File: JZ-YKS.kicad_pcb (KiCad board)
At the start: 2 copper layers, 50 x 50 mm, 37 parts, among them IC1 JZ4725, U1 PINHEAD30, U2 PINHEAD6, U3 PINHEAD8, X1 CRYSTAL, X2 CRYSTAL

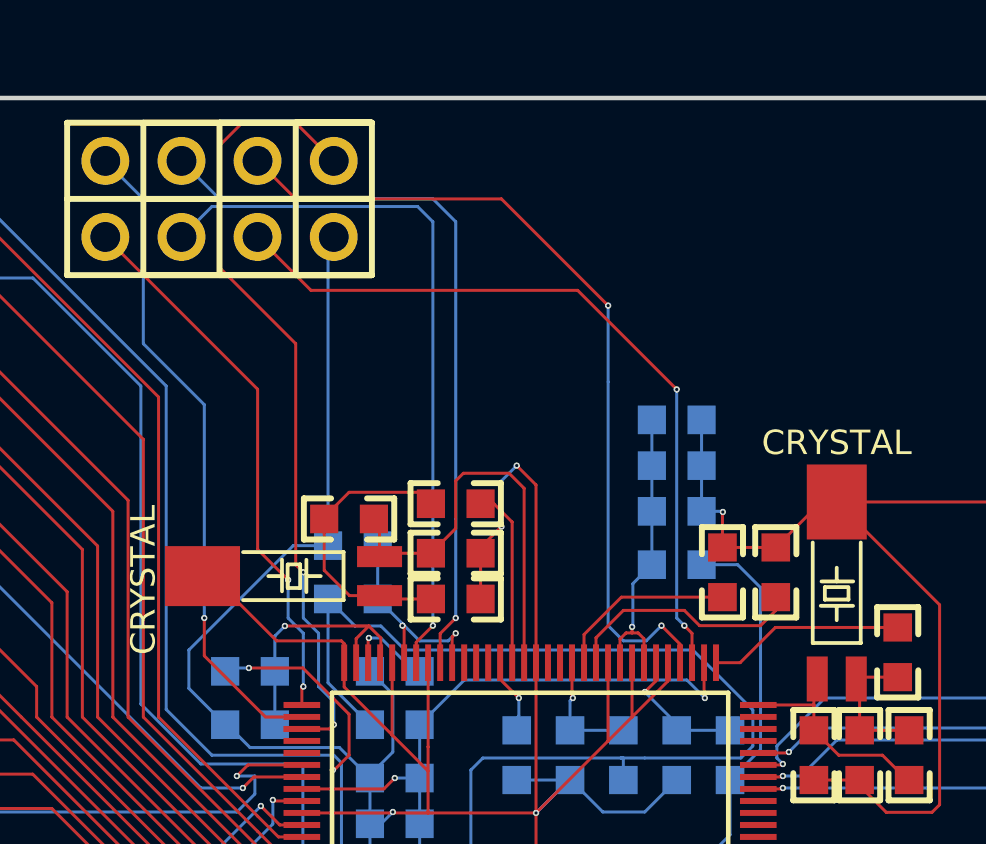
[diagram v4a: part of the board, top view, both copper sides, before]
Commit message: usb added
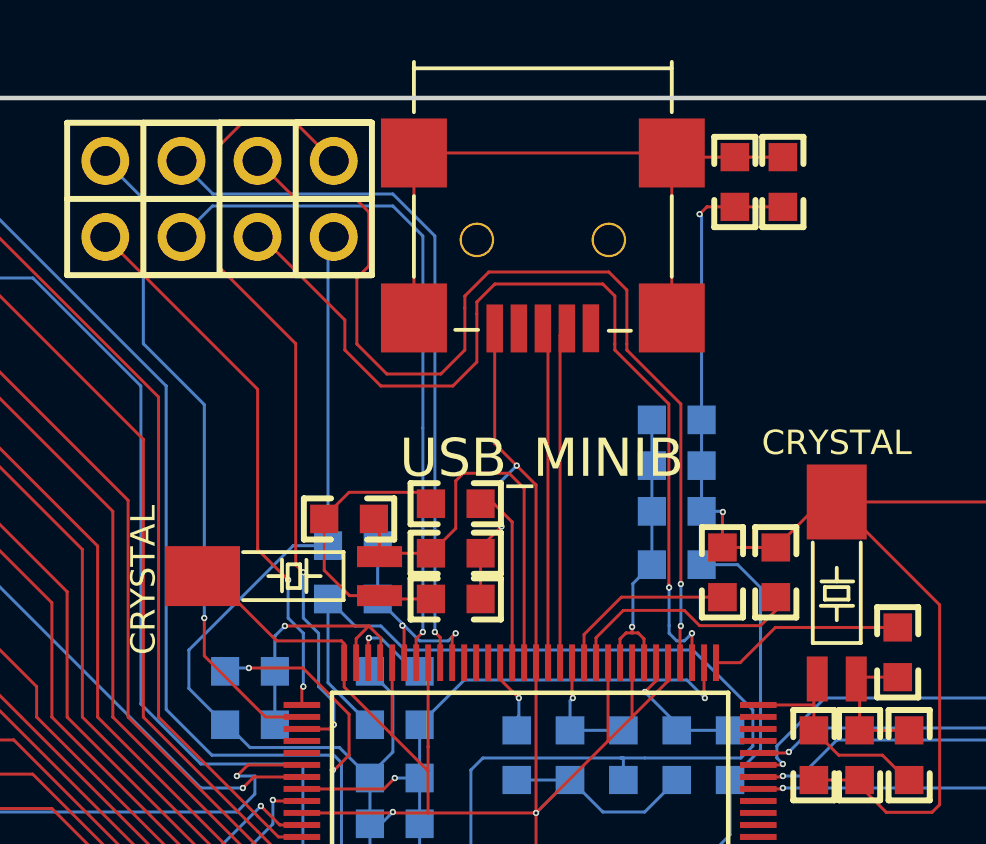
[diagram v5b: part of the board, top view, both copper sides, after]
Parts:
- added C20: CSMALL, size-0603, F.Cu at (218.6, 117.8)
- added FB8: FBSMALL, size-0603, F.Cu at (220.2, 117.8)
- added J1: USB_MINIB, CON_USB_MB, F.Cu at (212.2, 114.0)
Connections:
- IC1 pad 78: (no net) -> N-0000030
- IC1 pad 79: (no net) -> N-0000016
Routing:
- net N-0000029: track 0.00 -> 23.4 mm
- net GND: track 183.7 -> 198.3 mm, vias 5 -> 6
- net N-0000030: track 0.00 -> 11.2 mm
- net N-0000016: track 0.00 -> 11.2 mm
- net ADIN1: track 28.0 -> 34.3 mm
- net ADIN0: track 25.4 -> 31.2 mm
- net HP_R: track 24.9 -> 23.8 mm
- net HP_L: track 23.9 -> 23.2 mm
